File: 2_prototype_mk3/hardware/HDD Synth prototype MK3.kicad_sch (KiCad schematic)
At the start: 11 parts, among them SW1 SW_Push, U1 Optocoupler_DC_PhotoNPN_AKEC

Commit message: MKIII design refinements
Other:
- moved on the sheet: H4, H5
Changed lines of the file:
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@@
 	)
 	(junction
-		(at 60.96 151.13)
+		(at 43.18 166.37)
 		(diameter 0)
 		(color 0 0 0 0)
@@
 	(wire
 		(pts
-			(xy 74.93 144.78) (xy 74.93 151.13)
-		)
-		(stroke
-			(width 0)
-			(type default)
-		)
-	)
-	(wire
-		(pts
 			(xy 158.75 99.06) (xy 189.23 99.06)
 		)
@@
 	(wire
 		(pts
-			(xy 46.99 144.78) (xy 46.99 151.13)
-		)
-		(stroke
-			(width 0)
-			(type default)
-		)
-	)
-	(wire
-		(pts
 			(xy 228.6 93.98) (xy 228.6 96.52)
 		)
@@
 	(wire
 		(pts
+			(xy 43.18 166.37) (xy 43.18 171.45)
+		)
+		(stroke
+			(width 0)
+			(type default)
+		)
+	)
+	(wire
+		(pts
 			(xy 76.2 54.61) (xy 83.82 54.61)
 		)
@@
 	(wire
 		(pts
+			(xy 39.37 166.37) (xy 43.18 166.37)
+		)
+		(stroke
+			(width 0)
+			(type default)
+		)
+	)
+	(wire
+		(pts
 			(xy 191.77 123.19) (xy 191.77 125.73)
 		)
@@
 	(wire
 		(pts
-			(xy 74.93 151.13) (xy 60.96 151.13)
-		)
-		(stroke
-			(width 0)
-			(type default)
-		)
-	)
-	(wire
-		(pts
 			(xy 57.15 69.85) (xy 57.15 71.12)
 		)
@@
 	(wire
 		(pts
+			(xy 39.37 160.02) (xy 39.37 166.37)
+		)
+		(stroke
+			(width 0)
+			(type default)
+		)
+	)
+	(wire
+		(pts
 			(xy 53.34 78.74) (xy 113.03 78.74)
 		)
@@
 		(pts
 			(xy 251.46 92.71) (xy 251.46 93.98)
-		)
-		(stroke
-			(width 0)
-			(type default)
-		)
-	)
-	(wire
-		(pts
-			(xy 46.99 151.13) (xy 60.96 151.13)
 		)
 		(stroke
@@
 	(symbol
 		(lib_id "Mechanical:MountingHole_Pad")
-		(at 74.93 142.24 0)
+		(at 39.37 157.48 0)
 		(unit 1)
 		(exclude_from_sim no)
@@
 		(fields_autoplaced yes)
 		(property "Reference" "H5"
-			(at 77.47 139.6999 0)
+			(at 41.91 154.9399 0)
 			(effects
 				(font
@@
 		)
 		(property "Value" "MountingHole_Pad"
-			(at 77.47 142.2399 0)
+			(at 41.91 157.4799 0)
 			(effects
 				(font
@@
 		)
 		(property "Footprint" "MountingHole:MountingHole_3.2mm_M3_Pad_Via"
-			(at 74.93 142.24 0)
+			(at 39.37 157.48 0)
 			(effects
 				(font
@@
 		)
 		(property "Datasheet" "~"
-			(at 74.93 142.24 0)
+			(at 39.37 157.48 0)
 			(effects
 				(font
@@
 		)
 		(property "Description" "Mounting Hole with connection"
-			(at 74.93 142.24 0)
+			(at 39.37 157.48 0)
 			(effects
 				(font
@@
 	(symbol
 		(lib_id "Mechanical:MountingHole_Pad")
-		(at 46.99 142.24 0)
+		(at 43.18 163.83 0)
 		(unit 1)
 		(exclude_from_sim no)
@@
 		(fields_autoplaced yes)
 		(property "Reference" "H4"
-			(at 49.53 139.6999 0)
+			(at 45.72 161.2899 0)
 			(effects
 				(font
@@
 		)
 		(property "Value" "MountingHole_Pad"
-			(at 49.53 142.2399 0)
+			(at 45.72 163.8299 0)
 			(effects
 				(font
@@
 		)
 		(property "Footprint" "MountingHole:MountingHole_3.2mm_M3_Pad_Via"
-			(at 46.99 142.24 0)
+			(at 43.18 163.83 0)
 			(effects
 				(font
@@
 		)
 		(property "Datasheet" "~"
-			(at 46.99 142.24 0)
+			(at 43.18 163.83 0)
 			(effects
 				(font
@@
 		)
 		(property "Description" "Mounting Hole with connection"
-			(at 46.99 142.24 0)
+			(at 43.18 163.83 0)
 			(effects
 				(font
@@
 	(symbol
 		(lib_id "power:GND")
-		(at 60.96 151.13 0)
+		(at 43.18 171.45 0)
 		(unit 1)
 		(exclude_from_sim no)
@@
 		(fields_autoplaced yes)
 		(property "Reference" "#PWR05"
-			(at 60.96 157.48 0)
+			(at 43.18 177.8 0)
 			(effects
 				(font
@@
 		)
 		(property "Value" "GND"
-			(at 60.96 156.21 0)
+			(at 43.18 176.53 0)
 			(effects
 				(font
@@
 		)
 		(property "Footprint" ""
-			(at 60.96 151.13 0)
+			(at 43.18 171.45 0)
 			(effects
 				(font
@@
 		)
 		(property "Datasheet" ""
-			(at 60.96 151.13 0)
+			(at 43.18 171.45 0)
 			(effects
 				(font
@@
 		)
 		(property "Description" "Power symbol creates a global label with name \"GND\" , ground"
-			(at 60.96 151.13 0)
-			(effects
-				(font
+			(at 43.18 171.45 0)
+			(effects
+				(font

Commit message: Add net classes for power
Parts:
- removed Pot1: R_Potentiometer, Potentiometer_THT:Potentiometer_Alps_RK09K_Single_Horizontal, symbol Device:R_Potentiometer
- added H10, H11, H12, H13, H14, H7, H8, H9: MountingHole, MountingHole:MountingHole_3.2mm_M3, symbol Mechanical:MountingHole
- added Q1: 2N3904, Package_TO_SOT_SMD:SOT-23, symbol Transistor_BJT:2N3904
- added R4: 10K, Resistor_SMD:R_0603_1608Metric, symbol Device:R_Small
- added R7: 3.3K, Resistor_SMD:R_0603_1608Metric, symbol Device:R
- added SW2: RotaryEncoder_Switch, Rotary_Encoder:RotaryEncoder_Bourns_Horizontal_PEC12R-2x17F-Sxxxx, symbol Device:RotaryEncoder_Switch
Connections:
- net GND: now also Q1.1 (E), R7.2, SW2.C, SW2.S2
- net IDE_ACTIVITY: now also R7.1
- net ENC_A: now reaches A1.26 (GPIO20)
- net ENC_A: now also SW2.A
- net ENC_B: now reaches A1.27 (GPIO21)
- net ENC_B: now also SW2.B
- net ENC_SWITCH: now reaches A1.29 (GPIO22)
- net ENC_SWITCH: now also SW2.S1
- net at A1.30 (RUN): now also R4.2
- net VOL_POT: no longer names the net of A1.32 (GPIO27_ADC1)
- new net: Q1.3 (C), R4.1
- new net ISA IDE activity detection/RESET: Q1.2 (B)
- no-connect marks 15 -> 12
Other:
- sheet ISA IDE activity detection ports: added RESET; removed none
- sheet SD card reader ports: added SD_CS; removed SD_CI
- note added: "IDE is 5v Voltage dividor to 3v"
- note added: "Pico power reset (from ISA reset)"
- note added: "Rear bracket mounts"
- note added: "Speaker mounts (Large) Dimensions: 41x71x23mm Mounting holes (M3, centres: 33.5mm/63.5m)"
- note added: "Speaker mounts (Small) Dimensions: 40x40x20mm"
- note added: "Volume/balance encoder"
- note removed: "Originally used Potentiometer_THT:Potentiometer_Bourns_3386W_Horizontal which has the correct pins spacing, but no structural mount holes"
- note removed: "Volume control potentiometer"
- moved on the sheet: H4, H5, R1, R2

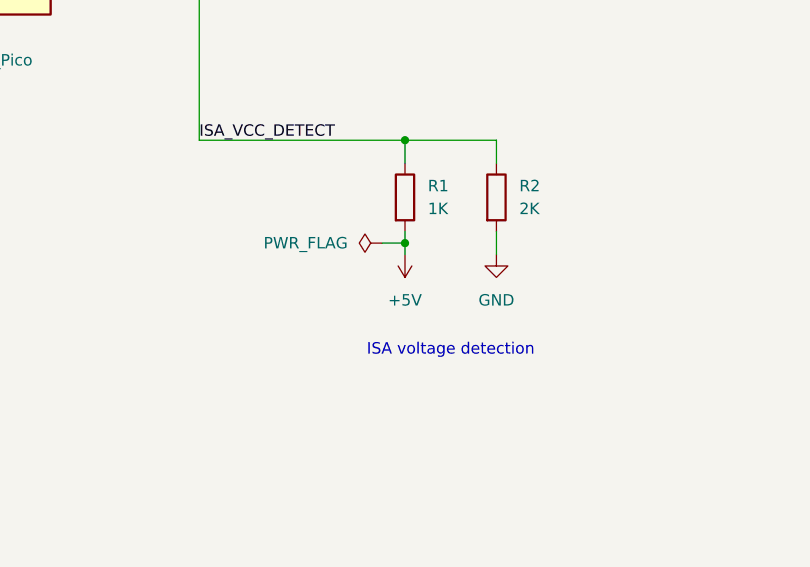
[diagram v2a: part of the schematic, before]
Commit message: MKIII PCB components connected and passing DRC
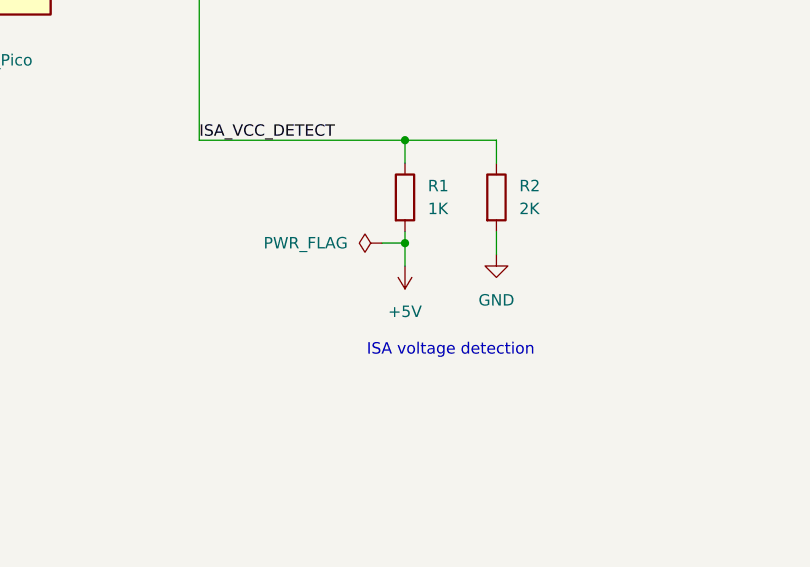
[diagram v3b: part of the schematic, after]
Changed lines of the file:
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@@
 	(wire
 		(pts
-			(xy 194.31 144.78) (xy 194.31 143.51)
+			(xy 194.31 143.51) (xy 194.31 146.05)
 		)
 		(stroke
@@
 		(length 2.54)
 		(shape round)
-		(at 130.81 43.18 90)
+		(at 194.31 143.51 90)
 		(fields_autoplaced yes)
 		(effects
@@
 		)
 		(property "Netclass" "POWER_5v"
+			(at 191.77 142.8115 90)
+			(effects
+				(font
+					(size 1.27 1.27)
+				)
+				(justify left)
+			)
+		)
+		(property "Component Class" ""
+			(at -43.18 5.08 0)
+			(effects
+				(font
+					(size 1.27 1.27)
+					(italic yes)
+				)
+			)
+		)
+	)
+	(netclass_flag ""
+		(length 2.54)
+		(shape round)
+		(at 130.81 43.18 90)
+		(fields_autoplaced yes)
+		(effects
+			(font
+				(size 1.27 1.27)
+			)
+			(justify left bottom)
+		)
+		(property "Netclass" "POWER_5V_SUP"
 			(at 128.27 42.4815 90)
 			(effects
@@
 				(path "/5a2f0aa7-670f-4d0d-8d56-ad98c847383a"
 					(reference "H12")
-					(unit 1)
-				)
-			)
-		)
-	)
-	(symbol
-		(lib_id "power:+5V")
-		(at 194.31 144.78 0)
-		(mirror x)
-		(unit 1)
-		(exclude_from_sim no)
-		(in_bom yes)
-		(on_board yes)
-		(dnp no)
-		(property "Reference" "#PWR04"
-			(at 194.31 140.97 0)
-			(effects
-				(font
-					(size 1.27 1.27)
-				)
-				(hide yes)
-			)
-		)
-		(property "Value" "+5V"
-			(at 194.31 149.86 0)
-			(effects
-				(font
-					(size 1.27 1.27)
-				)
-			)
-		)
-		(property "Footprint" ""
-			(at 194.31 144.78 0)
-			(effects
-				(font
-					(size 1.27 1.27)
-				)
-				(hide yes)
-			)
-		)
-		(property "Datasheet" ""
-			(at 194.31 144.78 0)
-			(effects
-				(font
-					(size 1.27 1.27)
-				)
-				(hide yes)
-			)
-		)
-		(property "Description" "Power symbol creates a global label with name \"+5V\""
-			(at 194.31 144.78 0)
-			(effects
-				(font
-					(size 1.27 1.27)
-				)
-				(hide yes)
-			)
-		)
-		(pin "1"
-		)
-		(instances
-			(project ""
-				(path "/5a2f0aa7-670f-4d0d-8d56-ad98c847383a"
-					(reference "#PWR04")
 					(unit 1)
 				)
@@
 					(unit 1)
 				)
+			)
+		)
+	)
+	(symbol
+		(lib_id "power:+5V")
+		(at 194.31 146.05 180)
+		(unit 1)
+		(exclude_from_sim no)
+		(in_bom yes)
+		(on_board yes)
+		(dnp no)
+		(fields_autoplaced yes)
+		(property "Reference" "#PWR04"
+			(at 194.31 142.24 0)
+			(effects
+				(font
+					(size 1.27 1.27)
+				)
+				(hide yes)
+			)
+		)
+		(property "Value" "+5V"
+			(at 194.31 151.13 0)
+			(effects
+				(font
+					(size 1.27 1.27)
+				)
+			)
+		)
+		(property "Footprint" ""
+			(at 194.31 146.05 0)
+			(effects
+				(font
+					(size 1.27 1.27)
+				)
+				(hide yes)
+			)
+		)
+		(property "Datasheet" ""
+			(at 194.31 146.05 0)
+			(effects
+				(font
+					(size 1.27 1.27)
+				)
+				(hide yes)
+			)
+		)
+		(property "Description" "Power symbol creates a global label with name \"+5V\""
+			(at 194.31 146.05 0)
+			(effects
+				(font
+					(size 1.27 1.27)
+				)
+				(hide yes)
+			)
+		)
+		(pin "1"
+		)
+		(instances
+			(project ""
+				(path "/5a2f0aa7-670f-4d0d-8d56-ad98c847383a"
+					(reference "#PWR04")
+					(unit 1)
+				)

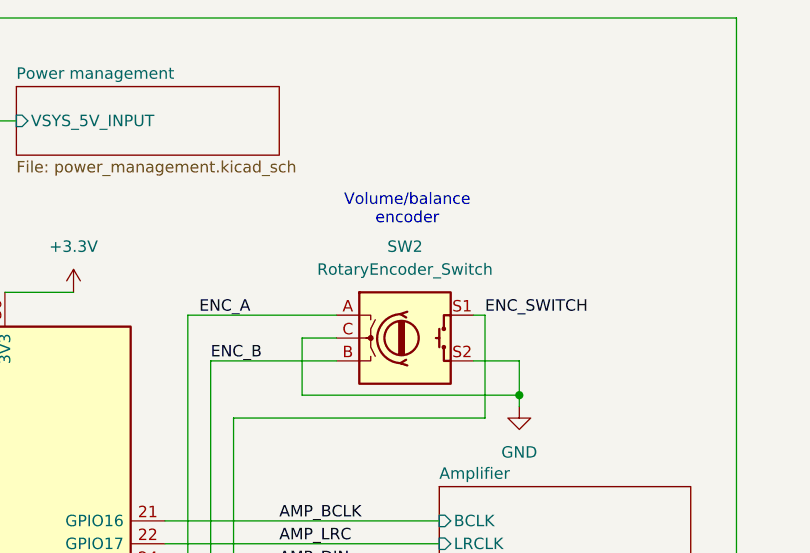
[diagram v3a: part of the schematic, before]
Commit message: Switch to GPLv3 licence
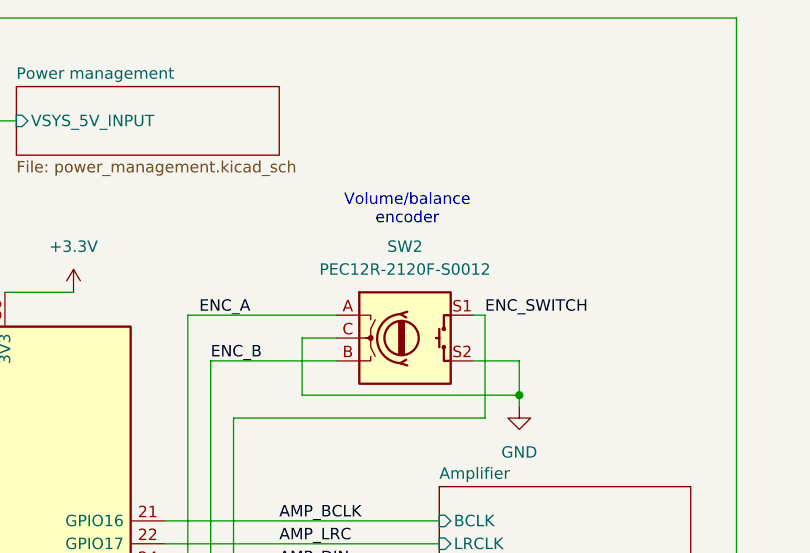
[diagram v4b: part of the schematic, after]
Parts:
- SW2: value RotaryEncoder_Switch -> PEC12R-2120F-S0012
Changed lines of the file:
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@@
 			)
 		)
-		(property "Value" "RotaryEncoder_Switch"
+		(property "Value" "PEC12R-2120F-S0012"
 			(at 185.42 45.72 0)
 			(effects
@@
 			)
 		)
-		(property "Datasheet" "~"
+		(property "Datasheet" "https://www.bourns.com/docs/Product-Datasheets/PEC12R.pdf"
 			(at 185.42 46.736 0)
 			(effects

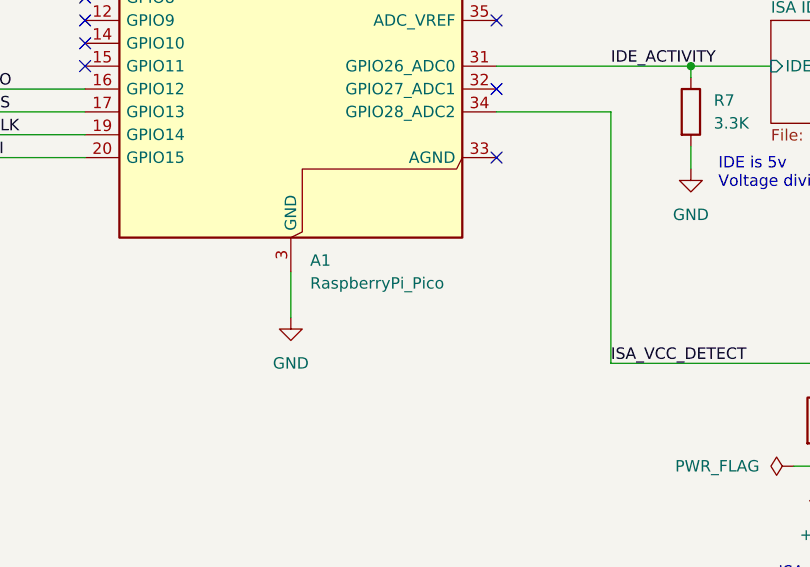
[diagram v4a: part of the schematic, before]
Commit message: Add manufacturer part nu bers
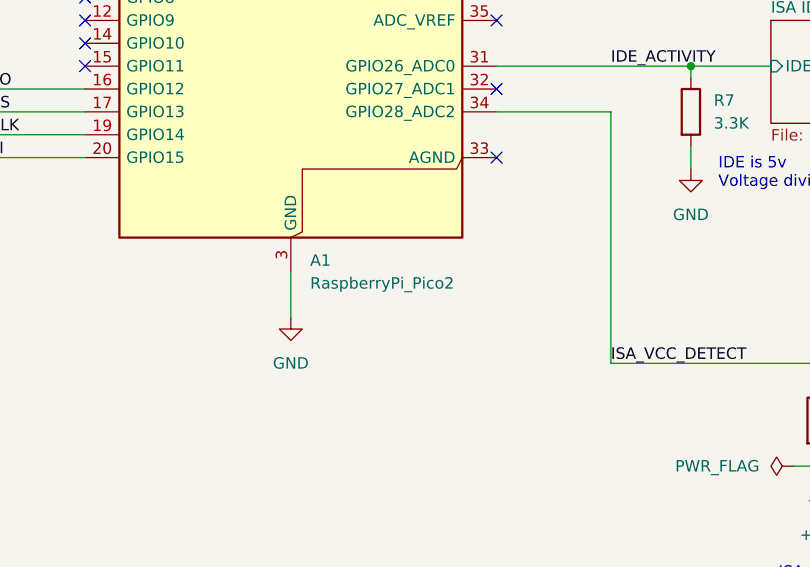
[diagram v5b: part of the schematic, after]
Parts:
- A1: value RaspberryPi_Pico -> RaspberryPi_Pico2; Manufacturer_Part_Number (none) -> SC1308
- Q1: Manufacturer_Part_Number (none) -> MMBT3904LT1G
- R1: Manufacturer_Part_Number (none) -> RC0603FR-071KL
- R2: Manufacturer_Part_Number (none) -> RC0603FR-072KL
- R4: Manufacturer_Part_Number (none) -> RC0603FR-0710KL
- R5: Manufacturer_Part_Number (none) -> RC0603FR-07330RL
- R7: Manufacturer_Part_Number (none) -> RC0603FR-073K3L
- SW1: Manufacturer_Part_Number (none) -> PTS645VL582LFS
- SW2: Manufacturer_Part_Number (none) -> PEC12R-2120F-S0012
- U1: Manufacturer_Part_Number (none) -> EL357N(C)(TA)-VG
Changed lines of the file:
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@@
+			)
+		)
+		(property "Manufacturer_Part_Number" ""
+			(at 88.9 179.07 0)
+			(effects
+				(font
+					(size 1.27 1.27)
+				)
+				(hide yes)
 			)
 		)
@@
 			)
 		)
+		(property "Manufacturer_Part_Number" ""
+			(at 58.42 184.15 0)
+			(effects
+				(font
+					(size 1.27 1.27)
+				)
+				(hide yes)
+			)
+		)
 		(instances
 			(project "HDD Synth prototype MK3"
@@
 			)
 		)
+		(property "Manufacturer_Part_Number" ""
+			(at 25.4 185.42 0)
+			(effects
+				(font
+					(size 1.27 1.27)
+				)
+				(hide yes)
+			)
+		)
 		(pin "1"
 		)
@@
 			)
 		)
+		(property "Manufacturer_Part_Number" "RC0603FR-072KL"
+			(at 204.47 138.43 0)
+			(effects
+				(font
+					(size 1.27 1.27)
+				)
+				(hide yes)
+			)
+		)
 		(pin "2"
 		)
@@
 			)
 		)
+		(property "Manufacturer_Part_Number" ""
+			(at 58.42 189.23 0)
+			(effects
+				(font
+					(size 1.27 1.27)
+				)
+				(hide yes)
+			)
+		)
 		(instances
 			(project "HDD Synth prototype MK3"
@@
 			)
 		)
+		(property "Manufacturer_Part_Number" "RC0603FR-0710KL"
+			(at 113.03 43.18 0)
+			(effects
+				(font
+					(size 1.27 1.27)
+				)
+				(hide yes)
+			)
+		)
 		(pin "2"
 		)
@@
 			)
 		)
+		(property "Manufacturer_Part_Number" "RC0603FR-071KL"
+			(at 194.31 138.43 0)
+			(effects
+				(font
+					(size 1.27 1.27)
+				)
+				(hide yes)
+			)
+		)
 		(pin "1"
 		)
@@
 			)
 		)
-		(property "Value" "RaspberryPi_Pico"
+		(property "Value" "RaspberryPi_Pico2"
 			(at 138.0333 123.19 0)
 			(effects
@@
 			)
 		)
+		(property "Manufacturer_Part_Number" "SC1308"
+			(at 135.89 86.36 0)
+			(effects
+				(font
+					(size 1.27 1.27)
+				)
+				(hide yes)
+			)
+		)
 		(pin "11"
 		)
@@
 			)
 		)
+		(property "Manufacturer_Part_Number" "PTS645VL582LFS"
+			(at 66.04 71.12 0)
+			(effects
+				(font
+					(size 1.27 1.27)
+				)
+				(hide yes)
+			)
+		)
 		(pin "1"
 		)
@@
 			)
 		)
+		(property "Manufacturer_Part_Number" ""
+			(at 88.9 189.23 0)
+			(effects
+				(font
+					(size 1.27 1.27)
+				)
+				(hide yes)
+			)
+		)
 		(instances
 			(project "HDD Synth prototype MK3"
@@
 			)
 		)
+		(property "Manufacturer_Part_Number" ""
+			(at 88.9 173.99 0)
+			(effects
+				(font
+					(size 1.27 1.27)
+				)
+				(hide yes)
+			)
+		)
 		(instances
 			(project "HDD Synth prototype MK3"
@@
 			)
 		)
+		(property "Manufacturer_Part_Number" ""
+			(at 25.4 175.26 0)
+			(effects
+				(font
+					(size 1.27 1.27)
+				)
+				(hide yes)
+			)
+		)
 		(pin "1"
 		)
@@
 			)
 		)
+		(property "Manufacturer_Part_Number" "RC0603FR-07330RL"
+			(at 88.9 52.07 90)
+			(effects
+				(font
+					(size 1.27 1.27)
+				)
+				(hide yes)
+			)
+		)
 		(pin "2"
 		)
@@
 			)
 		)
+		(property "Manufacturer_Part_Number" "PEC12R-2120F-S0012"
+			(at 185.42 53.34 0)
+			(effects
+				(font
+					(size 1.27 1.27)
+				)
+				(hide yes)
+			)
+		)
 		(pin "C"
 		)
@@
 		)
 		(property "Description" "Mounting Hole without connection"
+			(at 58.42 179.07 0)
+			(effects
+				(font
+					(size 1.27 1.27)
+				)
+				(hide yes)
+			)
+		)
+		(property "Manufacturer_Part_Number" ""
 			(at 58.42 179.07 0)
 			(effects
@@
 			)
 		)
+		(property "Manufacturer_Part_Number" "EL357N(C)(TA)-VG"
+			(at 241.3 91.44 0)
+			(effects
+				(font
+					(size 1.27 1.27)
+				)
+				(hide yes)
+			)
+		)
 		(pin "2"
 		)
@@
 			)
 		)
+		(property "Manufacturer_Part_Number" ""
+			(at 58.42 173.99 0)
+			(effects
+				(font
+					(size 1.27 1.27)
+				)
+				(hide yes)
+			)
+		)
 		(instances
 			(project ""
@@
 			)
 		)
+		(property "Manufacturer_Part_Number" "RC0603FR-073K3L"
+			(at 180.34 104.14 0)
+			(effects
+				(font
+					(size 1.27 1.27)
+				)
+				(hide yes)
+			)
+		)
 		(pin "2"
 		)
@@
 		)
 		(property "Description" "0.2A Ic, 40V Vce, Small Signal NPN Transistor, TO-92"
+			(at 105.41 31.75 0)
+			(effects
+				(font
+					(size 1.27 1.27)
+				)
+				(hide yes)
+			)
+		)
+		(property "Manufacturer_Part_Number" "MMBT3904LT1G"
 			(at 105.41 31.75 0)
 			(effects
@@
 			)
 		)
+		(property "Manufacturer_Part_Number" ""
+			(at 71.12 52.07 0)
+			(effects
+				(font
+					(size 1.27 1.27)
+				)
+				(hide yes)
+			)
+		)
 		(pin "1"
 		)
@@
 			)
 		)
+		(property "Manufacturer_Part_Number" ""
+			(at 256.54 90.17 0)
+			(effects
+				(font
+					(size 1.27 1.27)
+				)
+				(hide yes)
+			)
+		)
 		(pin "1"
 		)
@@
 			(at 88.9 184.15 0)
 			(effects
+				(font
+					(size 1.27 1.27)
+				)
+				(hide yes)
+			)
+		)
+		(property "Manufacturer_Part_Number" ""
+			(at 88.9 184.15 0)
+			(effects
